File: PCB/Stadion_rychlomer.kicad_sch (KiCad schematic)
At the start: 42 parts, among them J1 USB_B_Micro, J2 OLED I2C, J3 ICSP, J4 Conn_01x03_Pin, J5 WHEEL REED, J6 AUX ( Button / EGT / CHT ), J7 ENG RPM, U1 ATmega328P-M, U2 FT232RL, U3 LM1117MP-5.0, Y1 16MHz

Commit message: Fixed labels, added filtering caps, modified rpm sense
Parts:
- removed D7: Zener, symbol Device:D_Zener_Small
- removed R9: 10k, Resistor_SMD:R_0603_1608Metric, symbol Device:R_Small
- added C14: 100n, Capacitor_SMD:C_0603_1608Metric, symbol Device:C_Small
- added C15: 10n, Capacitor_SMD:C_0603_1608Metric, symbol Device:C_Small
- added D6: 1N4148W, Diode_SMD:D_SOD-123F, symbol AERO_Diode:1N4148W
- added D8: SMCJ85CA, Diode_SMD:D_SMC_Handsoldering, symbol AERO_Power_Protection:SMCJ85CA
- added Q1: 140817143200, Aero_Device:140817143200, symbol AERO_Device:140817143200
- added R10: 15k, Resistor_SMD:R_0603_1608Metric, symbol Device:R_Small
- added R9: 200R, Resistor_SMD:R_MELF_MMB-0207, symbol AERO_Resistor:R_200_1W_500V_MELF_High_Pulse
- R8: value 10k -> 15k
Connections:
- net +5V: now also R10.1
- net GND: now also C14.2, C15.2, D6.2 (A), D8.1 (A1), Q1.2, Q1.3
- net RX: now also U2.1 (TXD)
- net TX: now also U2.5 (RXD)
- net D4_AUX: now reaches J6.1 (Pin_1)
- net D4_AUX: now also U1.2 (PD4)
- net D5_AUX: now reaches J6.2 (Pin_2)
- net D5_AUX: now also U1.9 (PD5)
- net A0_AUX: now reaches J6.3 (Pin_3)
- net A0_AUX: now also C13.1, U1.23 (PC0)
- net A1_AUX: now reaches J6.4 (Pin_4)
- net A1_AUX: now also C12.1, U1.24 (PC1)
- net D_N: now reaches J1.2 (D-), TP2.1, U2.16 (USBD-)
- net D12/MISO_: now reaches J4.1 (Pin_1)
- net D12/MISO_: now also U1.16 (PB4)
- net D13/SCK_: now reaches J4.2 (Pin_2)
- net D13/SCK_: now also R4.1, U1.17 (PB5)
- net RESET_: now reaches J4.3 (Pin_3)
- net RESET_: now also C8.2, R1.1, U1.29 (~{RESET}/PC6), C14.1
- net XTAL2: now reaches U1.8 (XTAL2/PB7), Y1.1
- net XTAL1: now reaches U1.7 (XTAL1/PB6), Y1.3
- net D2_REED_: now reaches C11.1, U1.32 (PD2)
- net D2_REED_: now also J5.1 (Pin_1), R10.2
- net at R8.1: now also C15.1, D6.1 (K), Q1.1; no longer U1.1 (PD3)
- net at R8.2: now also D8.2 (A2), R9.1
- net D+: now reaches J1.3 (D+), TP1.1, U2.15 (USBD+)
- net D11/MOSI_: now reaches J3.2 (Pin_2)
- net D11/MOSI_: now also U1.15 (PB3)
- net I2C_SDA: now reaches J2.1 (Pin_1)
- net I2C_SDA: now also U1.28 (PC5)
- net I2C_SCL: now reaches J2.2 (Pin_2)
- net I2C_SCL: now also U1.27 (PC4)
- net D3_ENG_RPM: now reaches J7.1 (Pin_1)
- net D3_ENG_RPM: now also R9.2
- new net D3_ENG_RPM_ISOL: Q1.4, U1.1 (PD3)
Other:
- note added: "AUX doplnit ochrany"
- note added: "DPC817L-A-TR ma pouzdro SLM-4 , zjistit jestli neni mensi 140357145100 je v sop-4 Ta 85V TVS se muze zvolit i vetsi pokud by mela zabirat uz pri 85V, ale mam ji Ten 200R Je tam pro uplny extremy typu 2kV spicka nebo 200V RMS ani tam byt nemusi samotna tvs veme 600W spicku"
- note added: "ENG RPM zapojit pred usmernovac - pred zdroj"
- note added: "Reset spojenej s MCU pres 100n proc?"
- note removed: "5V"
- note removed: "A0 AUX"
- note removed: "A1 AUX"
- note removed: "D+"
- note removed: "D11/MOSI"
- note removed: "D12/MISO"
- note removed: "D13/SCK"
- note removed: "D2 REED"
- note removed: "D3 ENG RPM"
- note removed: "D4 AUX"
- note removed: "D5 AUX"
- note removed: "D_N"
- note removed: "GND"
- note removed: "I2C SCL"
- note removed: "I2C SDA"
- note removed: "RESET"
- note removed: "RX"
- note removed: "TX"
- note removed: "XTAL1"
- note removed: "XTAL2"
- moved on the sheet: C11, J7, R1, R2, R3, R8, Y1

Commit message: Round PCB V1
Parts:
- removed J5: WHEEL REED, symbol Connector:Conn_01x02_Pin
- added H1, H2, H3: 2mm, MountingHole:MountingHole_2.2mm_M2_ISO7380_Pad, symbol Mechanical:MountingHole_Pad
- added J5: SPÍD & PWR, Connector_PinHeader_2.54mm:PinHeader_1x04_P2.54mm_Vertical, symbol Connector:Conn_01x04_Pin
- D3: footprint (none) -> Diode_SMD:D_0603_1608Metric
- F1: footprint (none) -> Diode_SMD:D_0201_0603Metric
- J1: footprint (none) -> Connector_USB:USB_Micro-B_Molex-105017-0001
- J2: footprint (none) -> Connector_PinHeader_2.54mm:PinHeader_1x04_P2.54mm_Vertical
- J3, J4: footprint (none) -> Connector_PinHeader_2.54mm:PinHeader_1x03_P2.54mm_Vertical
- J6: value AUX ( Button / EGT / CHT ) -> AUX DDAA; footprint (none) -> Connector_PinHeader_2.54mm:PinHeader_1x04_P2.54mm_Vertical
- J7: footprint (none) -> Connector_PinHeader_2.54mm:PinHeader_1x02_P2.54mm_Vertical
- Q1: footprint Aero_Device:140817143200 -> OptoDevice:Panasonic_APV-AQY_SSOP-4_4.45x2.65mm_P1.27mm
- U1: value ATmega328P-M -> Mikroprofesor
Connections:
- net +5V: now also J5.2 (Pin_2); no longer D3.1 (K)
- net A0_AUX: now also J6.4 (Pin_4); no longer J6.3 (Pin_3)
- net A1_AUX: now also J6.3 (Pin_3); no longer J6.4 (Pin_4)
- net GND: now also H1.1, H2.1, H3.1, J5.4 (Pin_4)
- net VBUS: now also J5.3 (Pin_3)
- net VCC: now also D3.1 (K)
- net D2_REED_ renamed D2_SPD
- net D2_SPD: now also J5.1 (Pin_1)
- no-connect marks 0 -> 22
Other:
- note added: "USB je pro snoby, nebude na PCB"
- note added: "V IN"
- note removed: "Reset spojenej s MCU pres 100n proc?"

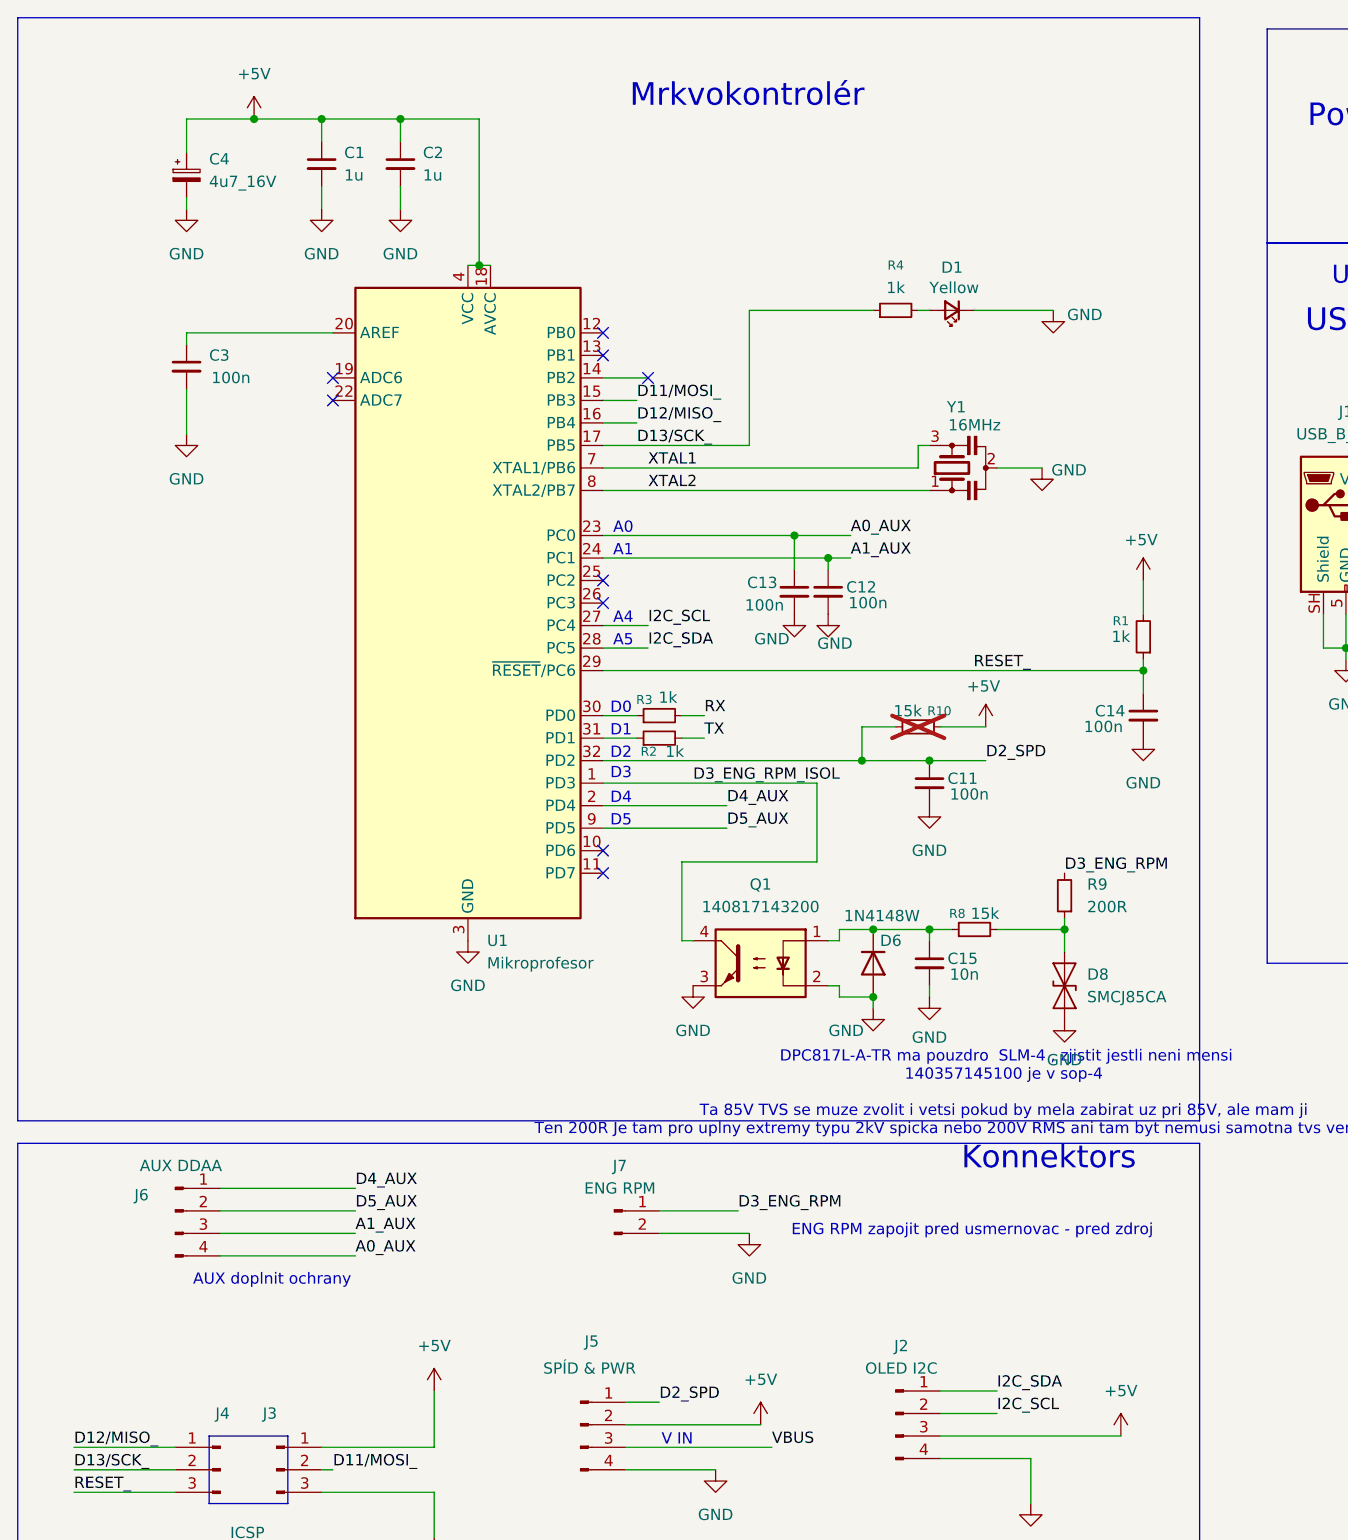
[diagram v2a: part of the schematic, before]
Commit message: SPD Optocoupler ESD Protection
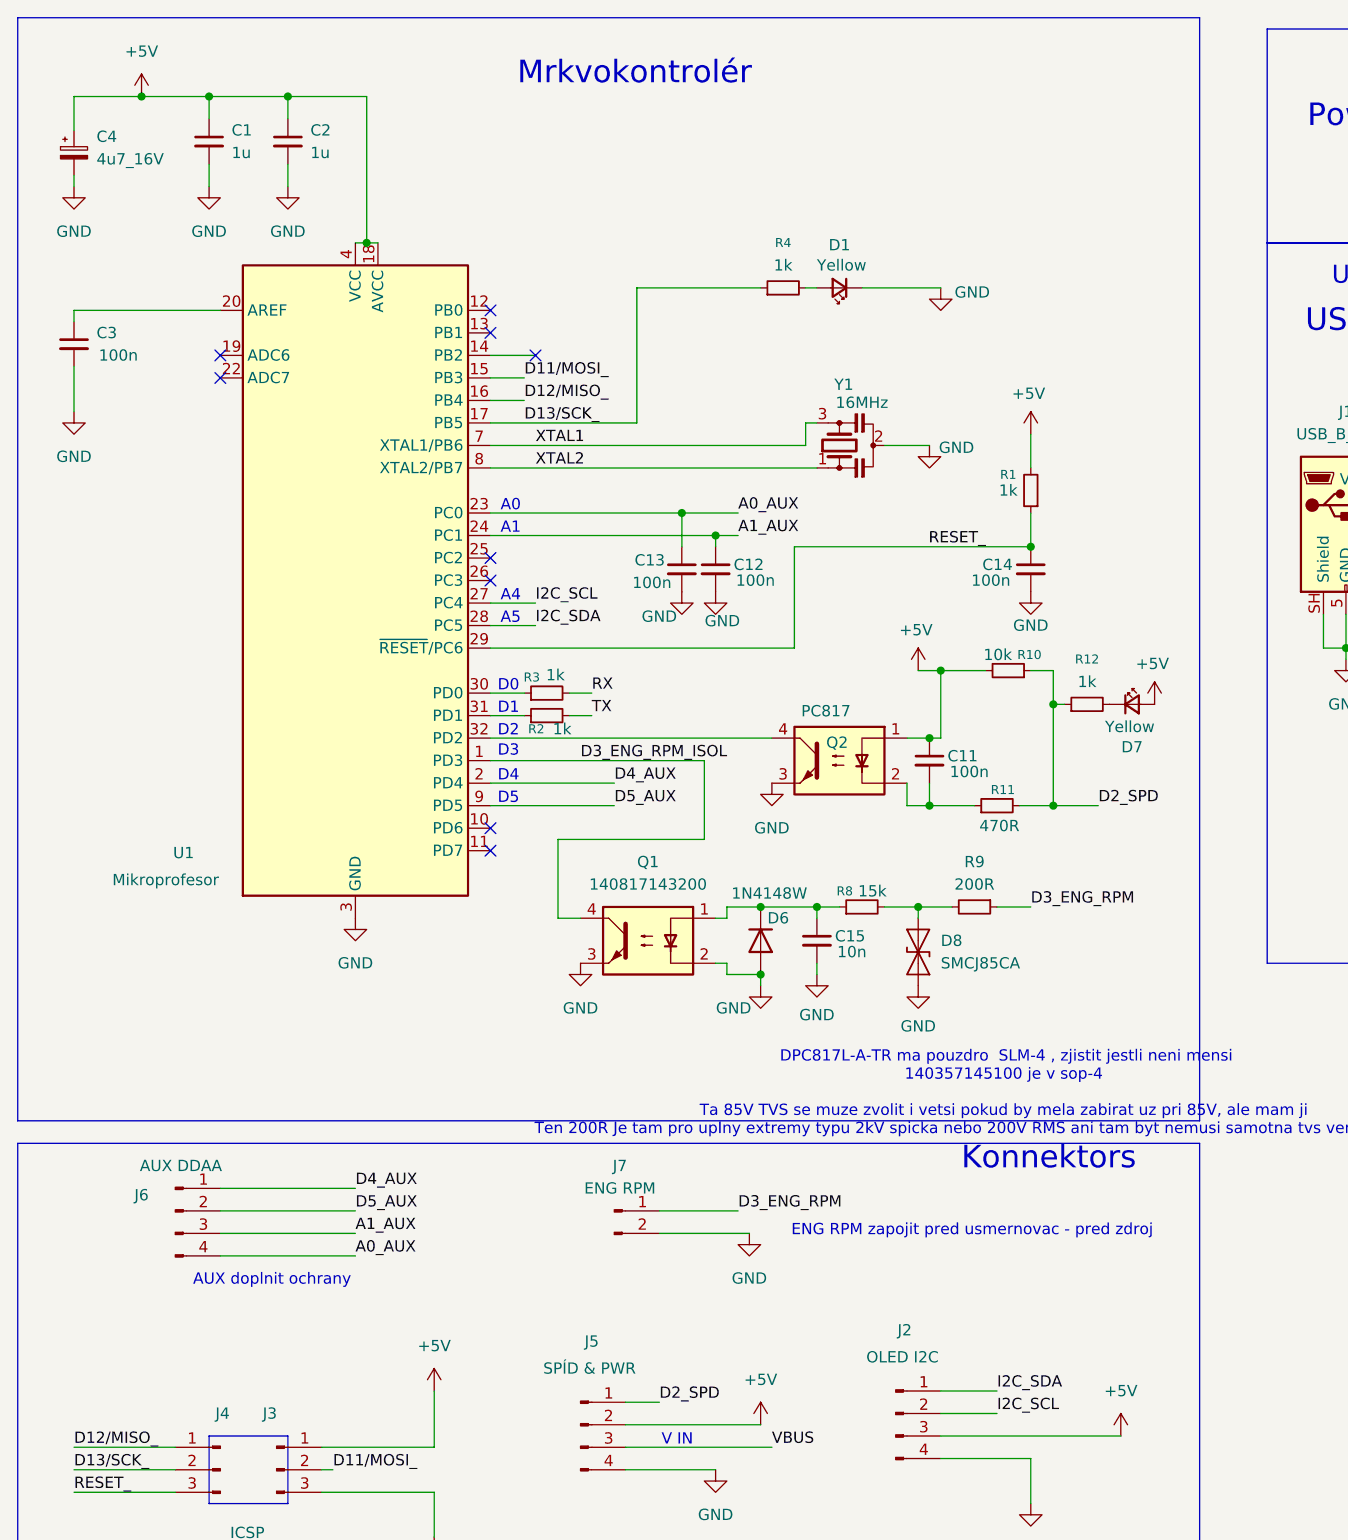
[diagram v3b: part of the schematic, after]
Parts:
- added D7: Yellow, LED_SMD:LED_0805_2012Metric, symbol Device:LED_Small
- added Q2: PC817, OptoDevice:Panasonic_APV-AQY_SSOP-4_4.45x2.65mm_P1.27mm, symbol AERO_Device:140817143200
- added R11: 470R, Resistor_SMD:R_0603_1608Metric, symbol Device:R_Small
- added R12: 1k, Resistor_SMD:R_0603_1608Metric, symbol Device:R_Small
- H1, H2, H3: footprint MountingHole:MountingHole_2.2mm_M2_ISO7380_Pad -> MountingHole:MountingHole_2.2mm_M2_Pad_Via
- R10: value 15k -> 10k; now fitted
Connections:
- net +5V: now also C11.1, R10.2, D7.2 (A), Q2.1; no longer R10.1
- net D2_SPD: now also R10.1, R11.2, R12.1; no longer C11.1, R10.2, U1.32 (PD2)
- net D3_ENG_RPM: now also R9.1; no longer R9.2
- net GND: now also Q2.3; no longer C11.2
- net at D8.2 (A2), R8.2: now also R9.2; no longer R9.1
- new net: C11.2, Q2.2, R11.1
- new net: Q2.4, U1.32 (PD2)
- new net: D7.1 (K), R12.2
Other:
- moved on the sheet: C1, C11, C12, C13, C14, C15, C2, C3, C4, D1, D6, D8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

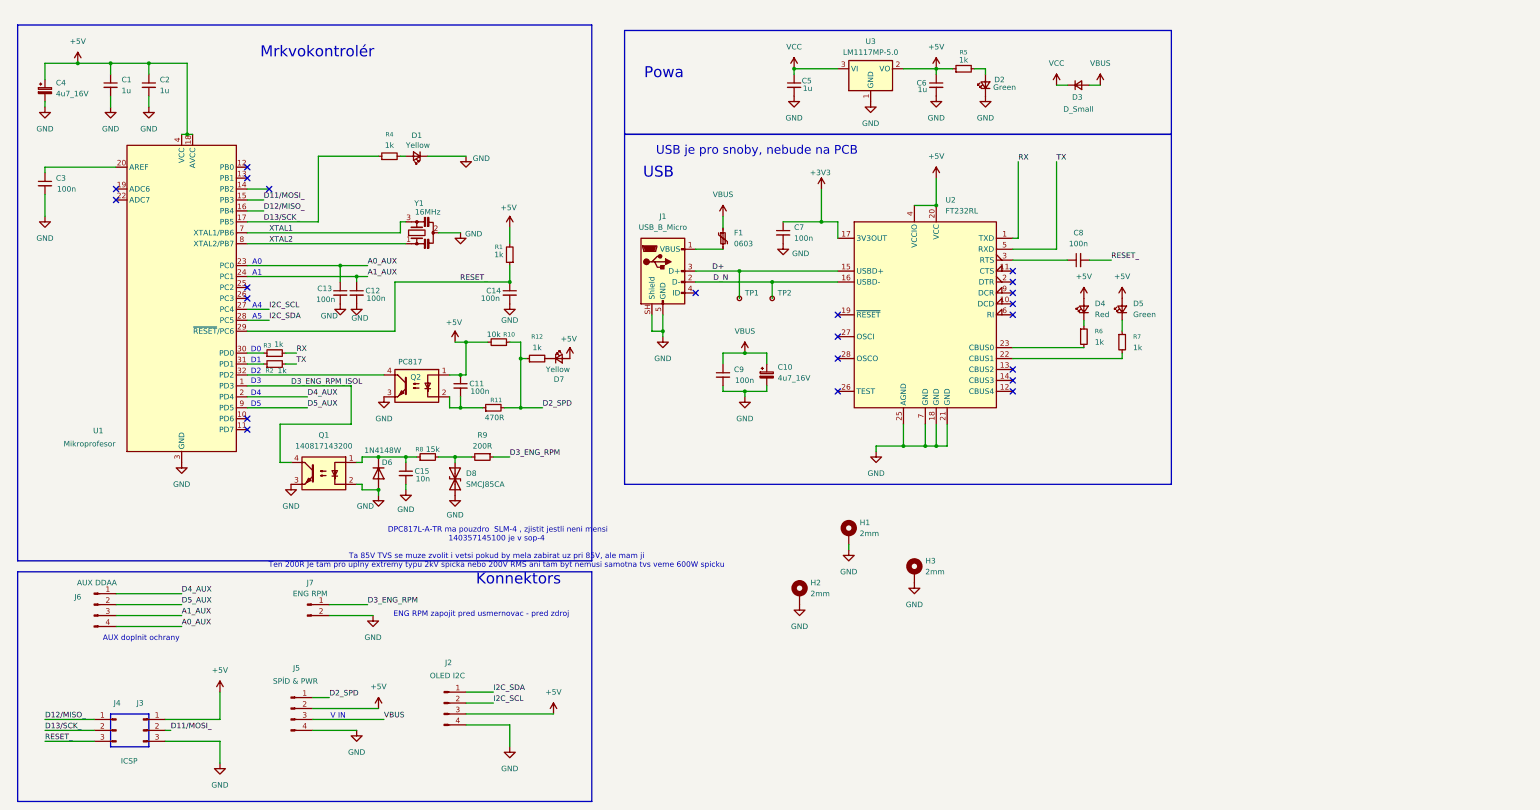
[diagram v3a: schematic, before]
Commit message: Ferrite beads add
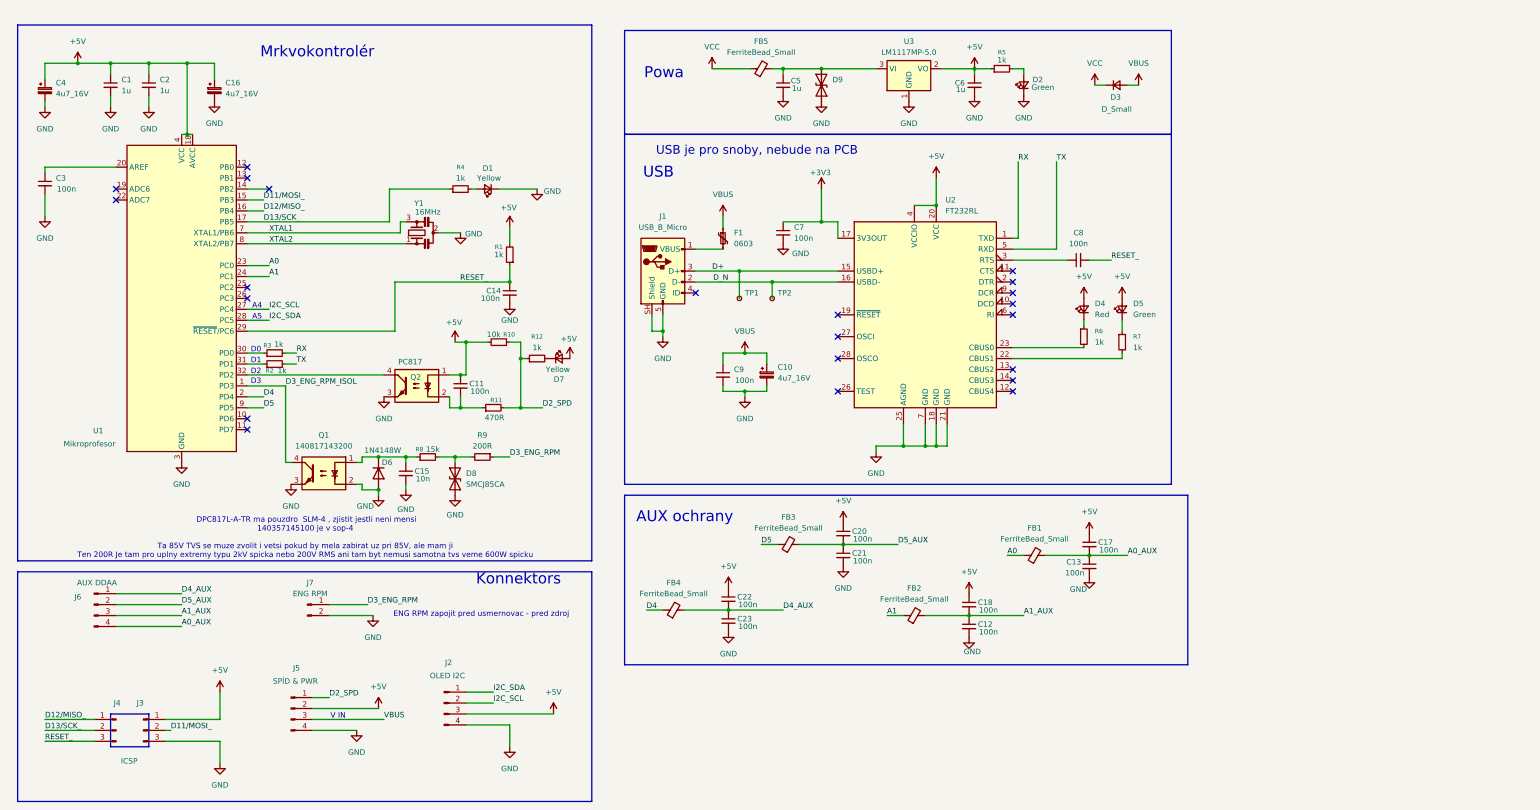
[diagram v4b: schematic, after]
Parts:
- removed H1, H2, H3: 2mm, MountingHole:MountingHole_2.2mm_M2_Pad_Via, symbol Mechanical:MountingHole_Pad
- added C16: 4u7_16V, Capacitor_Tantalum_SMD:CP_EIA-3216-10_Kemet-I, symbol Device:C_Polarized_Small
- added C17, C18, C20, C21, C22, C23: 100n, Capacitor_SMD:C_0603_1608Metric, symbol Device:C_Small
- added D9: SMCJ85CA, Diode_SMD:D_SOD-123F, symbol AERO_Power_Protection:SMCJ85CA
- added FB1, FB2, FB3, FB4: FerriteBead_Small, Inductor_SMD:L_Eaton_MCL2012V1, symbol Device:FerriteBead_Small
- added FB5: FerriteBead_Small, Inductor_SMD:L_Panasonic_PCC-M0530M, symbol Device:FerriteBead_Small
- D1, D7: JLCPCB Part (none) -> C2296
- D2: JLCPCB Part (none) -> C2297
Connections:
- net +5V: now also C16.1, C17.1, C18.1, C20.1, C22.1
- net A0_AUX: now also C17.2, FB1.2; no longer U1.23 (PC0)
- net A1_AUX: now also C18.2, FB2.2; no longer U1.24 (PC1)
- net D4_AUX: now also C22.2, C23.1, FB4.2; no longer U1.2 (PD4)
- net D5_AUX: now also C20.2, C21.1, FB3.2; no longer U1.9 (PD5)
- net GND: now also C16.2, C21.2, C23.2, D9.1 (A1)
- net VCC: now also FB5.1; no longer C5.1, U3.3 (VI)
- new net: C5.1, D9.2 (A2), FB5.2, U3.3 (VI)
- new net A0: FB1.1, U1.23 (PC0)
- new net A1: FB2.1, U1.24 (PC1)
- new net D4: FB4.1, U1.2 (PD4)
- new net D5: FB3.1, U1.9 (PD5)
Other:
- note added: "AUX ochrany"
- note removed: "A0"
- note removed: "A1"
- note removed: "AUX doplnit ochrany"
- note removed: "D4"
- note removed: "D5"
- moved on the sheet: C5, C6, D1, D2, D3, R4, R5, U3
